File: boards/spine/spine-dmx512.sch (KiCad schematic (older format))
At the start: 22 parts, among them P2 XLR-3 Female, Q1 IRFML8244, Q2 IRFML8244, T1 10/100baseT transformer, U4 NC7WZ14, U5 NC7WZ14, U6 NC7WZ14, U7 SN75176B

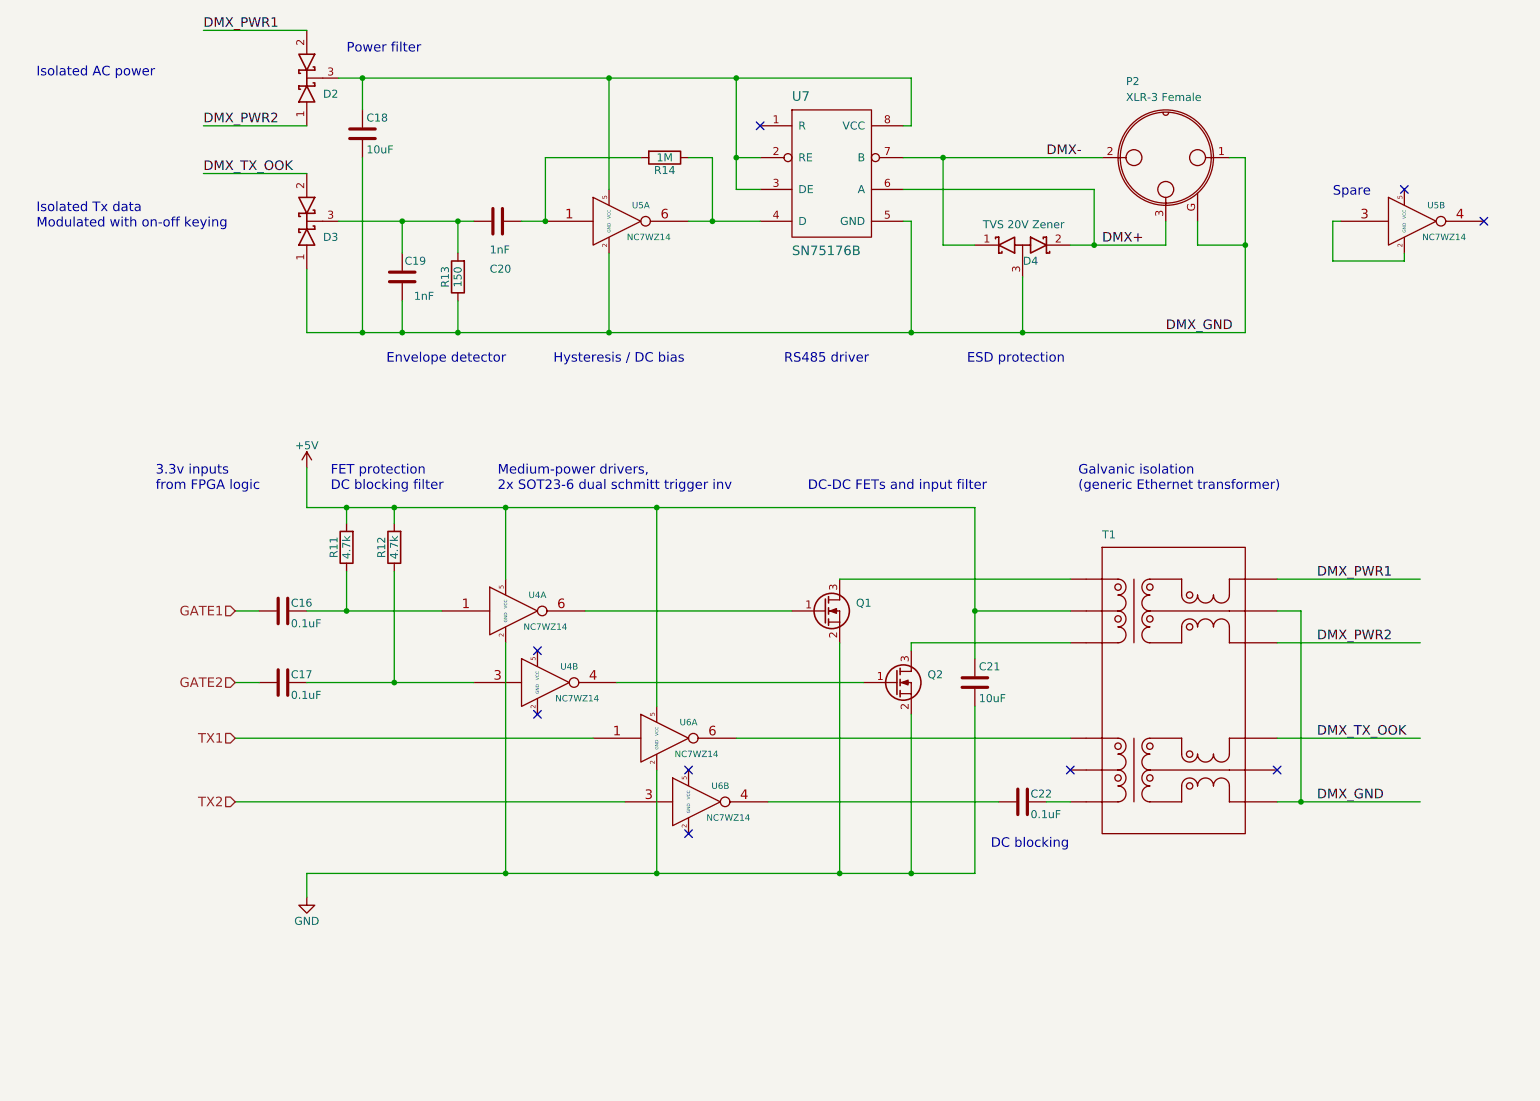
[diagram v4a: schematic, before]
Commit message: Getting the FPGA set up
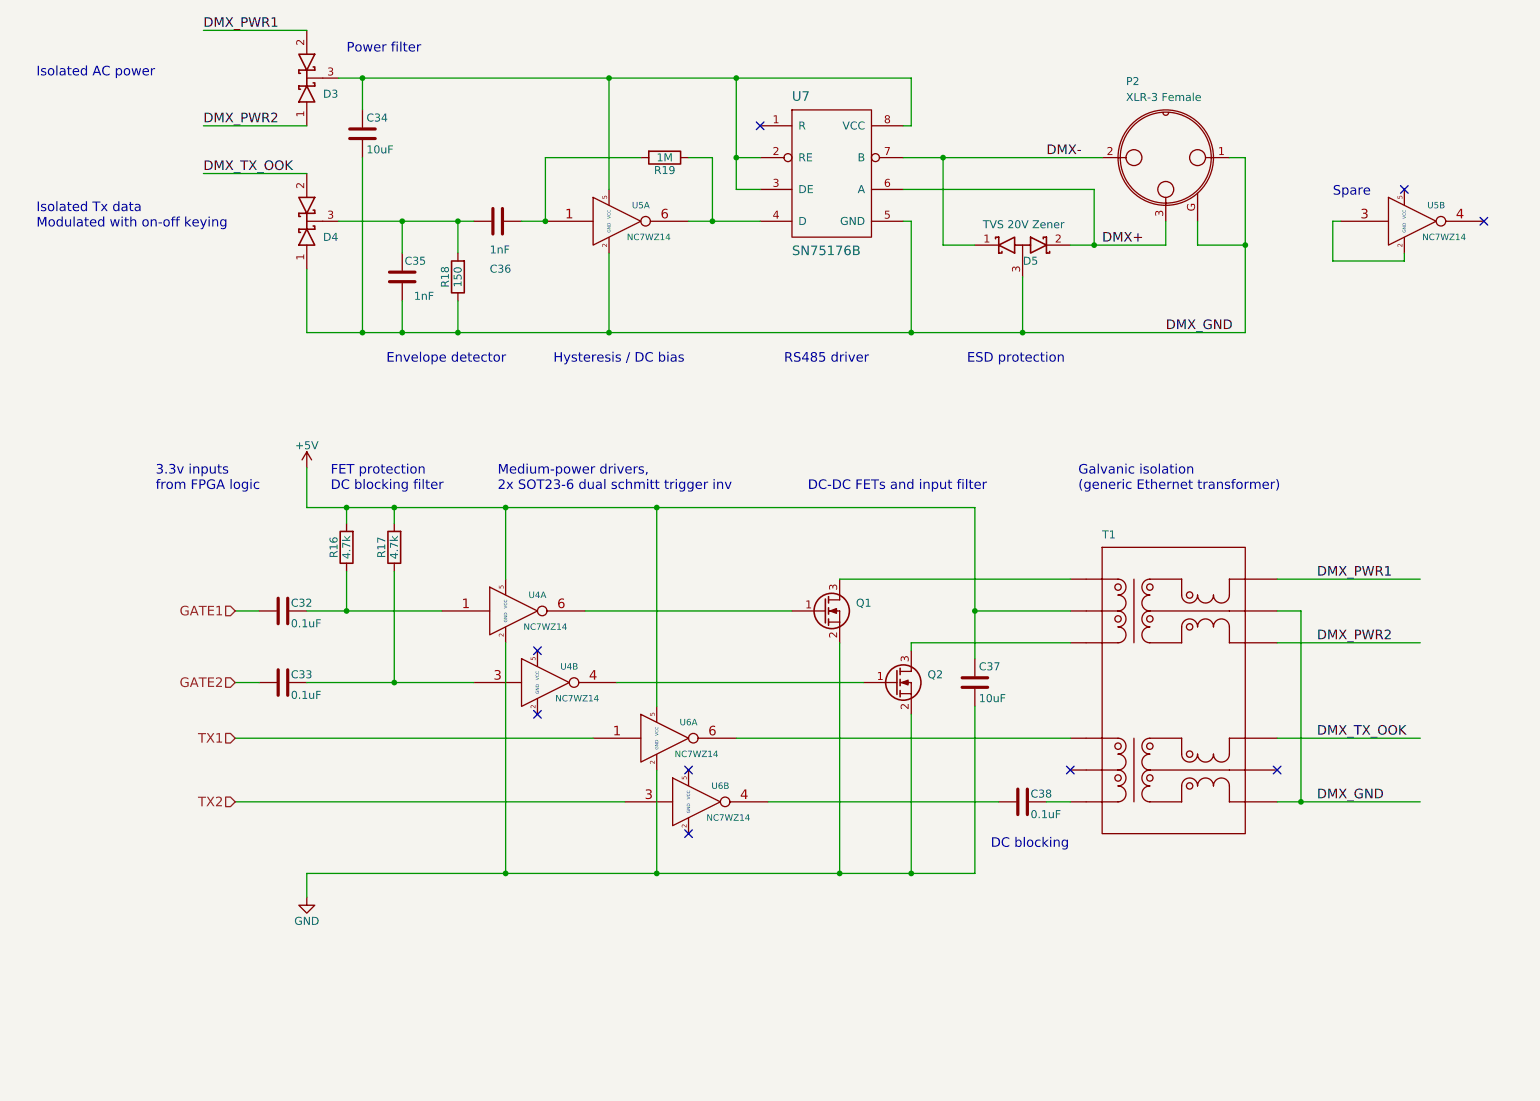
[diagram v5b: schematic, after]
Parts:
- renumbered C16 to C32, C17 to C33, C18 to C34, C19 to C35, C20 to C36, C21 to C37, C22 to C38, D2 to D3, D3 to D4, D4 to D5, R11 to R16, R12 to R17, R13 to R18, R14 to R19
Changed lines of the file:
@@
 $EndComp
 $Comp
-L D_Schottky_x2_ACom_KKA D4
+L D_Schottky_x2_ACom_KKA D5
 U 1 1 563E8FC2
 P 7100 2400
-F 0 "D4" H 7150 2300 50  0000 C CNN
+F 0 "D5" H 7150 2300 50  0000 C CNN
 F 1 "TVS 20V Zener" H 6850 2500 50  0000 L BNN
 F 2 "" H 7100 2400 60  0000 C CNN
@@
 NoConn ~ 9500 2050
 $Comp
-L R R14
+L R R19
 U 1 1 563ED073
 P 4850 1850
-F 0 "R14" V 4930 1850 50  0000 C CNN
+F 0 "R19" V 4930 1850 50  0000 C CNN
 F 1 "1M" V 4850 1850 50  0000 C CNN
 F 2 "" V 4780 1850 30  0000 C CNN
@@
 NoConn ~ 10000 2250
 $Comp
-L C C19
+L C C35
 U 1 1 563EDC1A
 P 3200 2600
-F 0 "C19" H 3050 2700 50  0000 L CNN
+F 0 "C35" H 3050 2700 50  0000 L CNN
 F 1 "1nF" H 3000 2450 50  0000 L BNN
 F 2 "" H 3238 2450 30  0000 C CNN
@@
 $EndComp
 $Comp
-L D_Schottky_x2_KCom_AAK D3
+L D_Schottky_x2_KCom_AAK D4
 U 1 1 563EE535
 P 2600 2250
-F 0 "D3" V 2500 2100 50  0000 C CNN
+F 0 "D4" V 2500 2100 50  0000 C CNN
 F 1 "BAT54 2x common cathode" H 2600 2350 50  0001 C CNN
 F 2 "" H 2600 2250 60  0000 C CNN
@@
 NoConn ~ 7400 5700
 $Comp
-L C C21
+L C C37
 U 1 1 563F0E74
 P 6800 5150
-F 0 "C21" H 6825 5250 50  0000 L CNN
+F 0 "C37" H 6825 5250 50  0000 L CNN
 F 1 "10uF " H 6825 5050 50  0000 L CNN
 F 2 "" H 6838 5000 30  0000 C CNN
@@
 $EndComp
 $Comp
-L GND #PWR017
+L GND #PWR33
 U 1 1 563F2AEF
 P 2600 6500
-F 0 "#PWR017" H 2600 6250 50  0001 C CNN
+F 0 "#PWR33" H 2600 6250 50  0001 C CNN
 F 1 "GND" H 2600 6350 50  0000 C CNN
 F 2 "" H 2600 6500 60  0000 C CNN
@@
 $EndComp
 $Comp
-L C C16
+L C C32
 U 1 1 563F4706
 P 2450 4700
-F 0 "C16" V 2400 4750 50  0000 L CNN
+F 0 "C32" V 2400 4750 50  0000 L CNN
 F 1 "0.1uF" V 2500 4750 50  0000 L TNN
 F 2 "" H 2488 4550 30  0000 C CNN
@@
 $EndComp
 $Comp
-L +5V #PWR018
+L +5V #PWR32
 U 1 1 563F515D
 P 2600 3800
-F 0 "#PWR018" H 2600 3650 50  0001 C CNN
+F 0 "#PWR32" H 2600 3650 50  0001 C CNN
 F 1 "+5V" H 2600 3940 50  0000 C CNN
 F 2 "" H 2600 3800 60  0000 C CNN
@@
 NoConn ~ 5000 6100
 $Comp
-L D_Schottky_x2_KCom_AAK D2
+L D_Schottky_x2_KCom_AAK D3
 U 1 1 563ED560
 P 2600 1350
-F 0 "D2" V 2500 1200 50  0000 C CNN
+F 0 "D3" V 2500 1200 50  0000 C CNN
 F 1 "BAT54 2x common cathode" H 2600 1450 50  0001 C CNN
 F 2 "" H 2600 1350 60  0000 C CNN
@@
 $EndComp
 $Comp
-L C C18
+L C C34
 U 1 1 563F1736
 P 2950 1700
-F 0 "C18" H 2975 1800 50  0000 L CNN
+F 0 "C34" H 2975 1800 50  0000 L CNN
 F 1 "10uF " H 2975 1600 50  0000 L CNN
 F 2 "" H 2988 1550 30  0000 C CNN
@@
 $EndComp
 $Comp
-L R R13
+L R R18
 U 1 1 563F3452
 P 3550 2600
-F 0 "R13" V 3630 2600 50  0000 C CNN
+F 0 "R18" V 3630 2600 50  0000 C CNN
 F 1 "150" V 3550 2600 50  0000 C CNN
 F 2 "" V 3480 2600 30  0000 C CNN
@@
 $EndComp
 $Comp
-L R R11
+L R R16
 U 1 1 563F362A
 P 2850 4300
-F 0 "R11" V 2930 4300 50  0000 C CNN
+F 0 "R16" V 2930 4300 50  0000 C CNN
 F 1 "4.7k" V 2850 4300 50  0000 C CNN
 F 2 "" V 2780 4300 30  0000 C CNN
@@
 $EndComp
 $Comp
-L R R12
+L R R17
 U 1 1 563F3881
 P 3150 4300
-F 0 "R12" V 3230 4300 50  0000 C CNN
+F 0 "R17" V 3230 4300 50  0000 C CNN
 F 1 "4.7k" V 3150 4300 50  0000 C CNN
 F 2 "" V 3080 4300 30  0000 C CNN
@@
 $EndComp
 $Comp
-L C C17
+L C C33
 U 1 1 563F48B8
 P 2450 5150
-F 0 "C17" V 2400 5200 50  0000 L CNN
+F 0 "C33" V 2400 5200 50  0000 L CNN
 F 1 "0.1uF" V 2500 5200 50  0000 L TNN
 F 2 "" H 2488 5000 30  0000 C CNN
@@
 $EndComp
 $Comp
-L C C22
+L C C38
 U 1 1 563F4920
 P 7100 5900
-F 0 "C22" V 7050 5950 50  0000 L CNN
+F 0 "C38" V 7050 5950 50  0000 L CNN
 F 1 "0.1uF" V 7150 5950 50  0000 L TNN
 F 2 "" H 7138 5750 30  0000 C CNN
@@
 $EndComp
 $Comp
-L C C20
+L C C36
 U 1 1 563F55AB
 P 3800 2250
-F 0 "C20" V 3500 2200 50  0000 L CNN
+F 0 "C36" V 3500 2200 50  0000 L CNN
 F 1 "1nF" V 3650 2200 50  0000 L BNN
 F 2 "" H 3838 2100 30  0000 C CNN

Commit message: Pick better capacitors :)
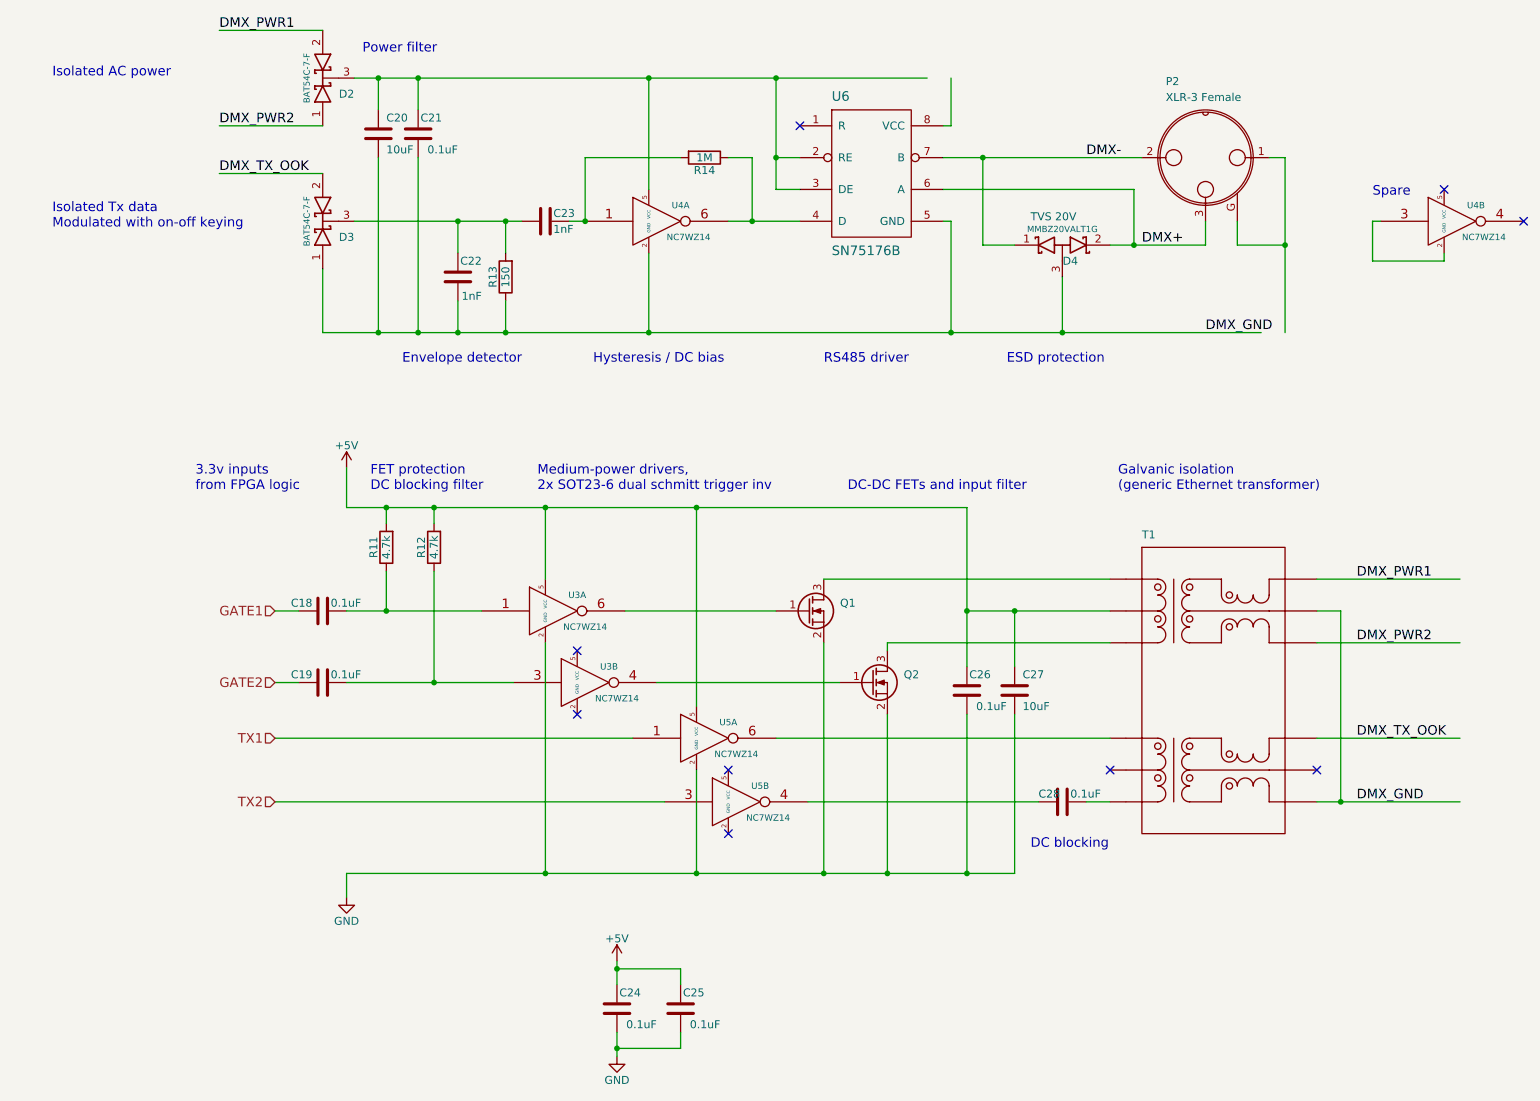
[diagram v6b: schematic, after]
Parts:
- removed C32, C33, C38: 0.1uF, symbol C
- removed C34, C37: 10uF, symbol C
- removed C36: 1nF, symbol C
- removed D3: BAT54 2x common cathode, symbol D_Schottky_x2_KCom_AAK
- added C18, C19, C21, C24, C25, C26, C28: 0.1uF, 0805, symbol C
- added C20, C27: 10uF, 1206, symbol C
- added C23: 1nF, 0805, symbol C
- added D2: BAT54 2x common cathode, symbol D_Schottky_x2_KCom_AAK
- C22: renamed from C35; footprint (none) -> 0805; MfgId CC0805KRX7R9BB102 -> GRM216R71H102KA01D; MfrId Yageo -> Murata; RefPrice1k 0.00981 -> 0.0156; Vend1Id 311-1127-1-ND -> 490-9741-1-ND
- D4: renamed from D5; value TVS 20V Zener -> TVS 20V
- renumbered D4 to D3, R16 to R11, R17 to R12, R18 to R13, R19 to R14, U4 to U3, U5 to U4, U6 to U5, U7 to U6
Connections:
- wire segments 81 -> 91
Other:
- moved on the sheet: C22, D3, D4, P2, Q1, Q2, R11, R12, R13, R14, T1, U3A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

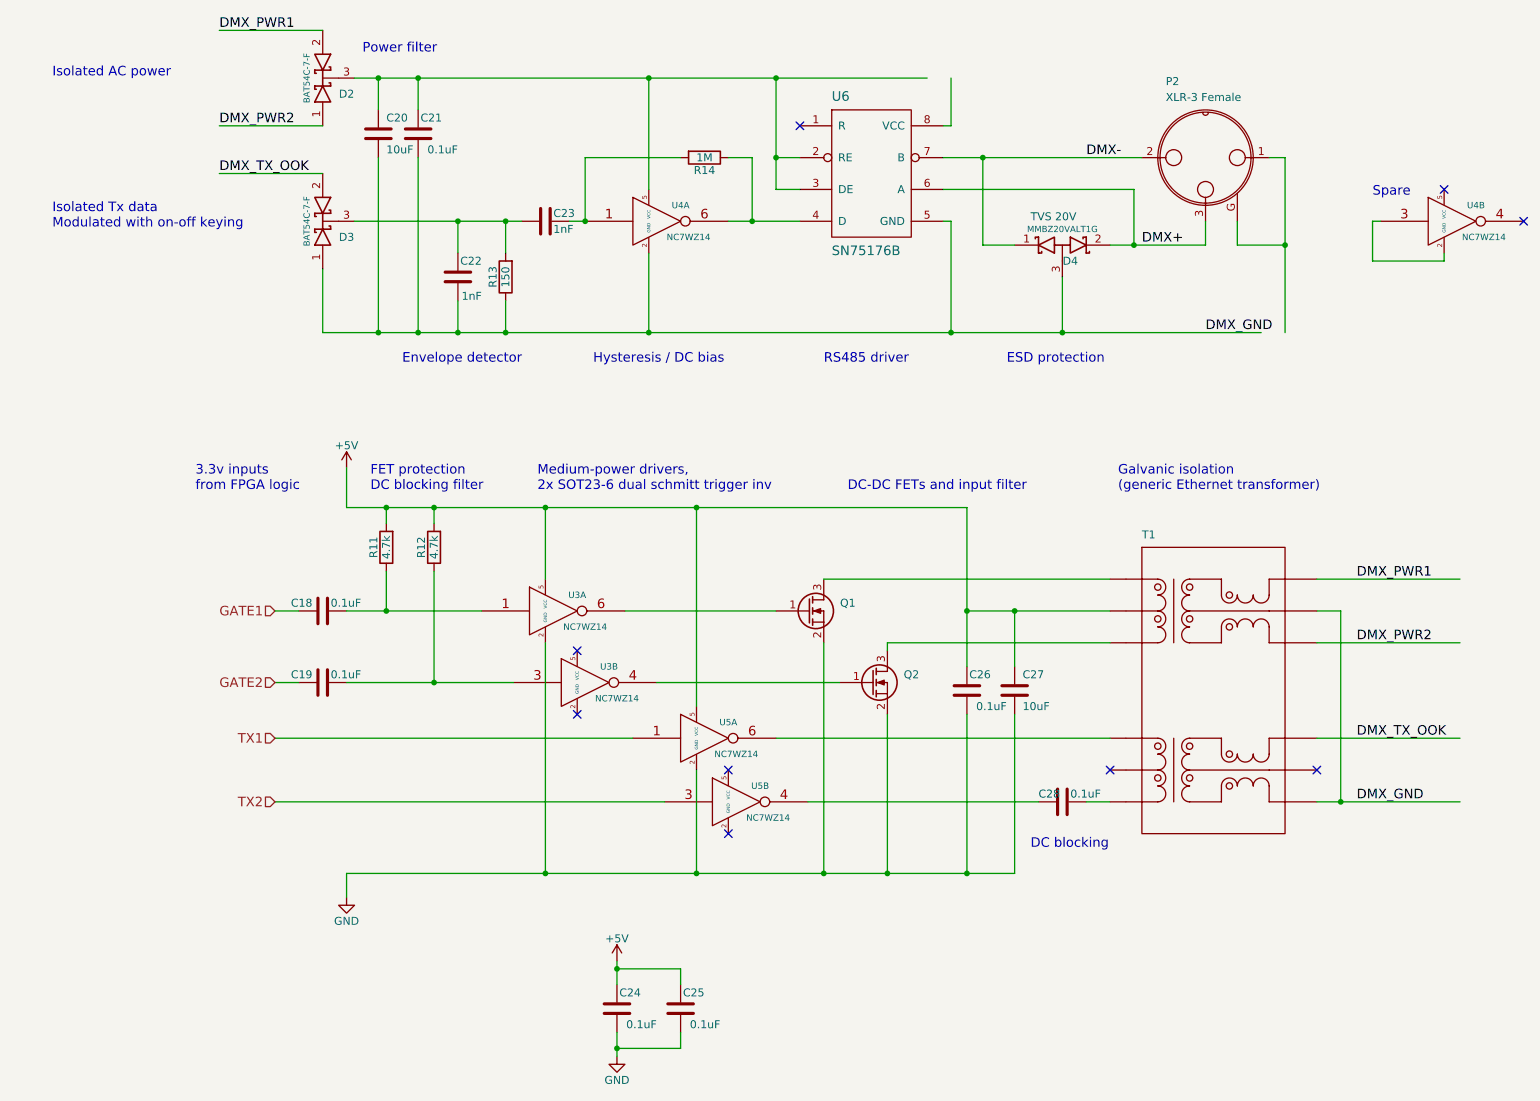
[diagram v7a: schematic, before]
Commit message: Split up the power schematic
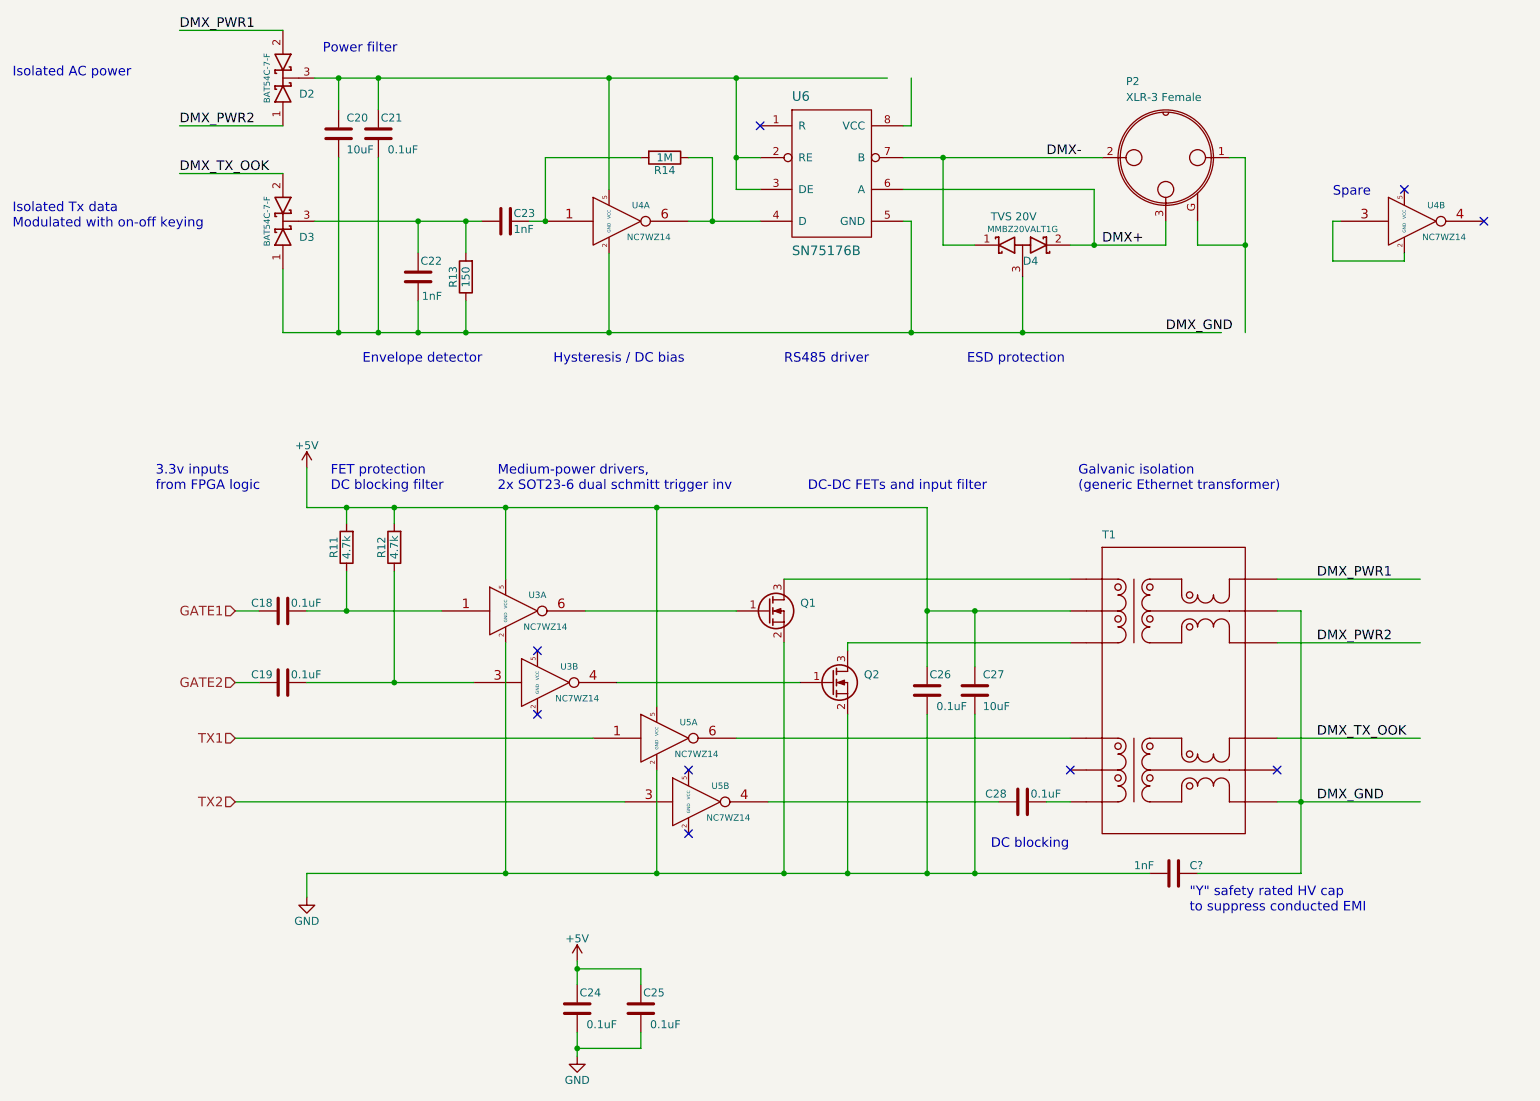
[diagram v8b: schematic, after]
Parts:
- added C?: 1nF, symbol C
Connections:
- wire segments 91 -> 92
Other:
- note added: ""Y" safety rated HV cap\nto suppress conducted EMI"
- moved on the sheet: C18, C19, C20, C21, C22, C23, C24, C25, C26, C27, C28, D2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
